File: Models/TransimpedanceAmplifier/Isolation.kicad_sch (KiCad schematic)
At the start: 2 parts

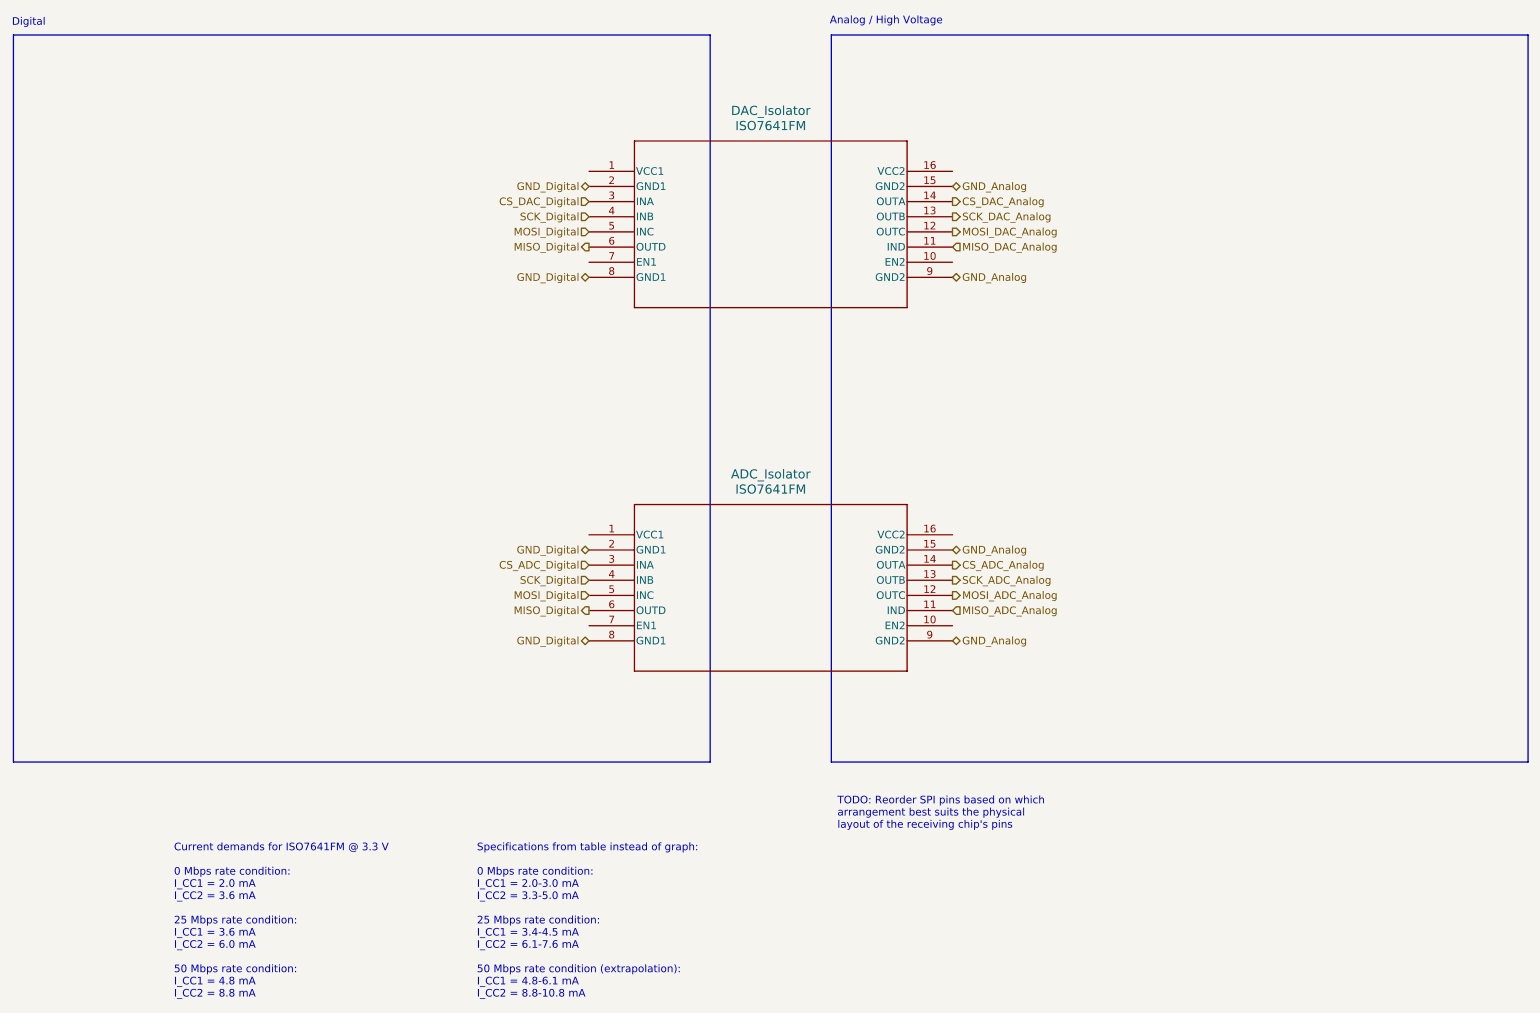
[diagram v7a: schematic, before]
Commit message: Patched the incorrect decoupling network for the isolators
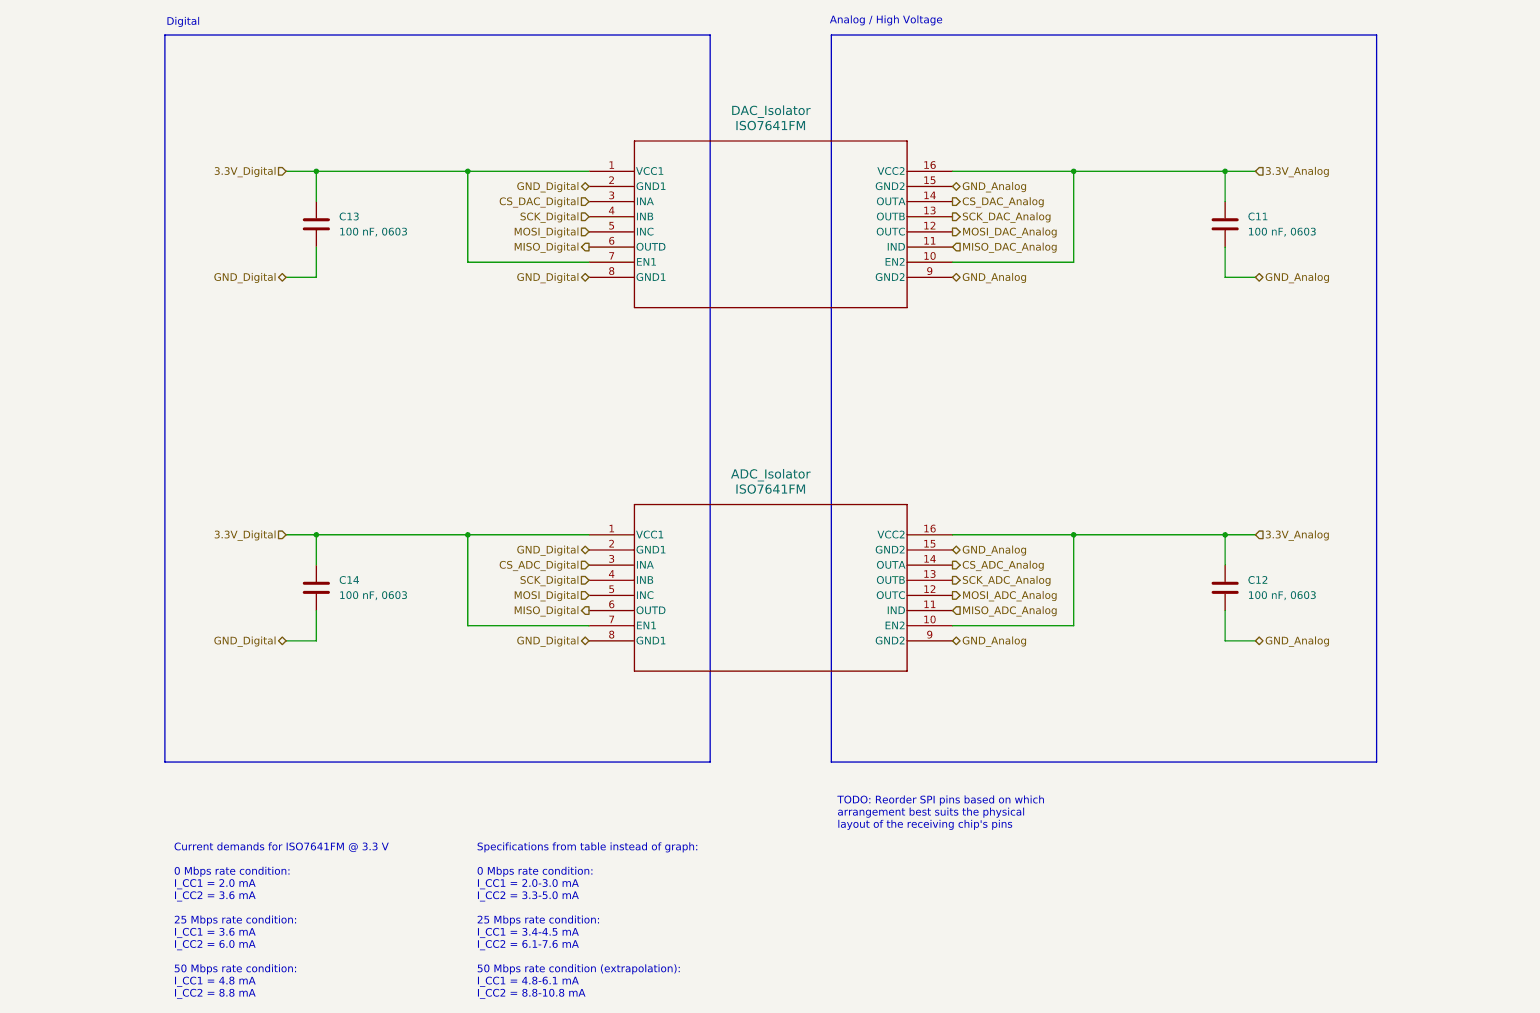
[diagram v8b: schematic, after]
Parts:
- added C11, C12, C13, C14: 100 nF, 0603, symbol Device:C
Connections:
- net GND_Analog: now also C11.2, C12.2
- net GND_Digital: now also C13.2, C14.2
- net 3.3V_Digital: now reaches ADC_Isolator.1 (VCC1)
- net 3.3V_Digital: now also ADC_Isolator.7 (EN1), DAC_Isolator.1 (VCC1), DAC_Isolator.7 (EN1), C13.1, C14.1
- net 3.3V_Analog: now reaches ADC_Isolator.10 (EN2)
- net 3.3V_Analog: now also ADC_Isolator.16 (VCC2), DAC_Isolator.10 (EN2), DAC_Isolator.16 (VCC2), C11.1, C12.1
